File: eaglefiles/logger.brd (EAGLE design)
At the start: 41 x 20.2 mm, 15 parts, among them IC2 MAX641CSA

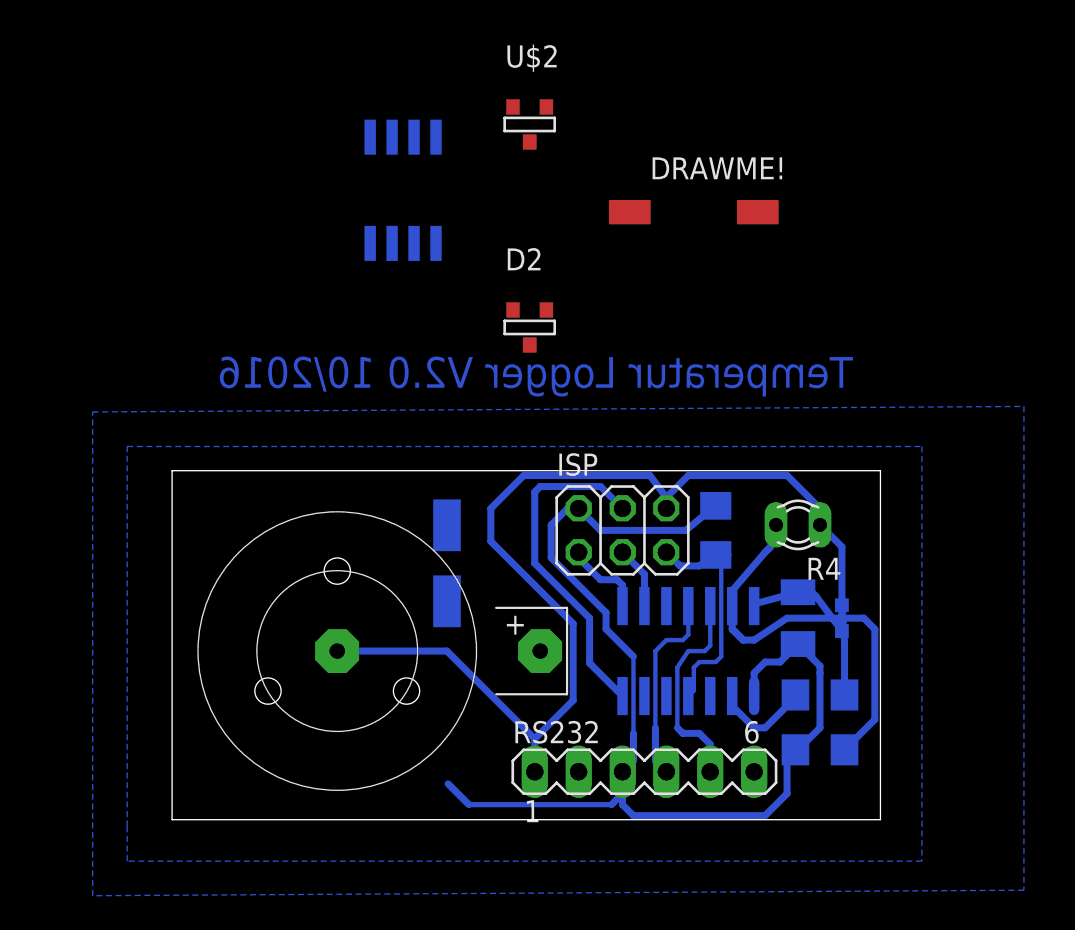
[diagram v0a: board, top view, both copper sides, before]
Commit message: UART-USB Adapter and TSIC-506 added
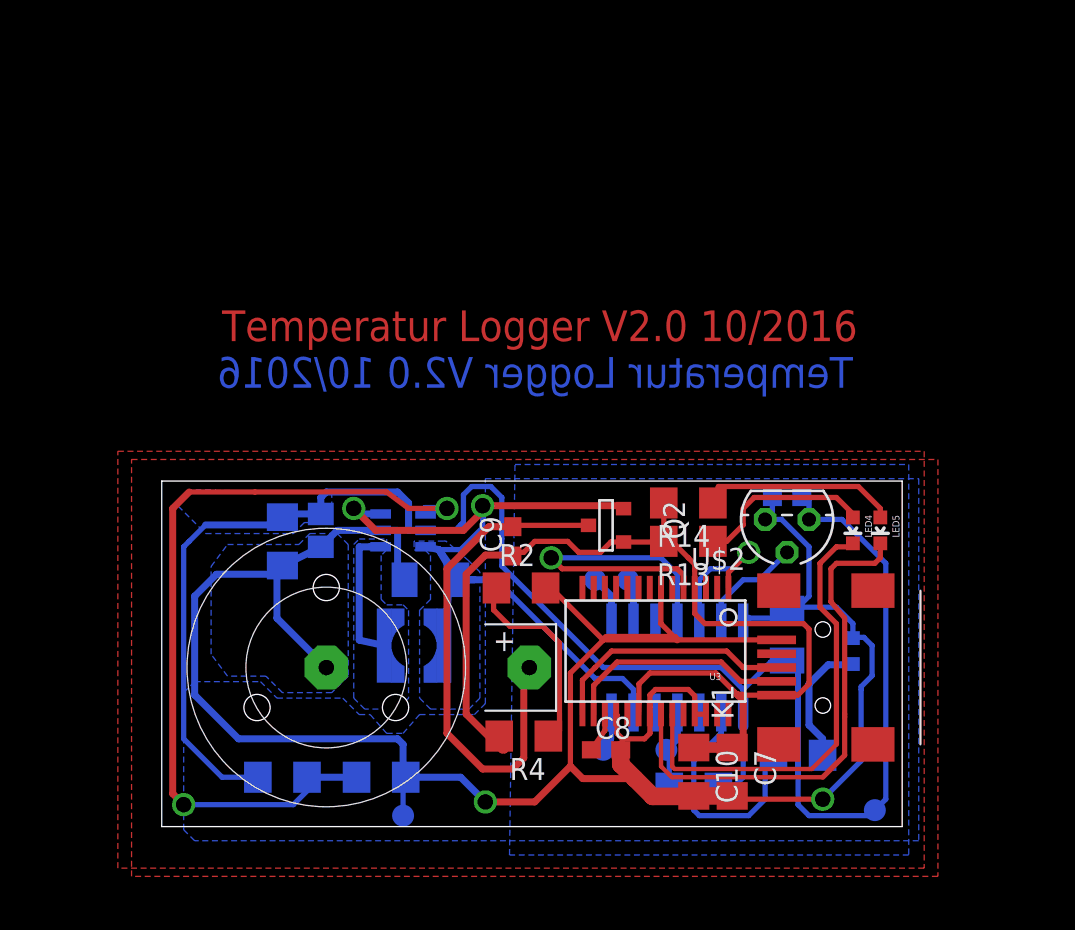
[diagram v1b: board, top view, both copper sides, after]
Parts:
- removed D2: BAV99, 0liver:SOT-23
- removed DRAWME!: 18uH, rcl:L8530M
- removed IC2: MAX641CSA, maxim:SO08
- removed ISP: (no value), pinhead:2X03
- removed RS232: (no value), con-lstb:MA06-1
- added C10: 10uF, rcl:C1206
- added C3: 4,7uF, rcl:C1206K
- added C4: 680nF, resistor:C0805
- added C5, C8, C9: 100nF, rcl:C0603
- added C7: 100nF, rcl:C1206
- added K1: 65100516121, Input-Output_Connectors_rev15d:65100516121
- added L1: 4,7uH, EagleLibrary_Wuerth_Elektronik_eiSos_rev16a:WE-TPC_3816
- added LED4: Red, SparkFun:LED-0603
- added LED5: Green, SparkFun:LED-0603
- added Q2: IRLML9301, 0liver:SOT-23
- added R13, R14: 1K, rcl:R1206
- added R5, R6: (no value), resistor:R1206
- added U$10, U$11, U$12, U$7, U$8, U$9: (no value), 0liver:PIN-1.27
- added U1: MCP1640, karlnet-parts:SOT23-6
- added U3: FT232RLSSOP, SparkFun:SSOP28DB
- C1: value 100uF -> 47uF; device rcl:153CLV-0505 -> resistor:C1206
- LED3: value (none) -> lc green; device led:SML0603 -> led:CHIPLED_0603
- R2: device rcl:R1206 -> eagle-ltspice:R1206
- R3: value 2k (calc!) -> 1,8k
- R4: value (none) -> 680; device ptc-ntc:P640 -> eagle-ltspice:R1206
- U$2: value IRLML6346 -> TSIC-506; device 0liver:SOT-23 -> 0liver:TO92
- moved U$2 27.3 mm to (36.2, 17.8), turned to 180 degrees
- moved R4 20.0 mm to (21.0, 5.24)
- moved R2 19.7 mm to (20.8, 13.8), flipped to the top
- moved R1 15.0 mm to (30.8, 2.22), turned to 180 degrees
- moved C1 9.61 mm to (6.99, 16.5), turned to 270 degrees
- moved R3 3.72 mm to (36.8, 4.13)
- moved LED3 2.01 mm to (40.0, 10.2), turned to 0 degrees
- moved IC1 1.14 mm to (29.8, 9.21)
- moved U$1 1.14 mm to (9.53, 9.21)
- moved C2 1.14 mm to (36.2, 11.1)
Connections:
- removed net D1: IC1.10, U$1.P$2
- removed net N$8: D2.3, DRAWME!.1, U$2.1
- new net 5V: R2.1, R4.1
- new net N$3: C8.1, U3.17
- new net N$4: LED4.A, R13.1
- new net N$6: C9.2, Q2.1, U$1.P$2
- new net RXLED: LED5.C, U3.22
- new net SW: L1.2, U1.1
- new net TXLED: LED4.C, U3.23
- new net USB_D+: K1.3, U3.15
- new net USB_D-: K1.2, U3.16
- new net VSUPPLY: C3.1, IC1.6, L1.1, Q2.2, U1.3, U1.6
- new net V_USB: C10.1, C7.1, C9.1, K1.1, Q2.3, R13.2, R14.2, R4.2, U3.20, U3.4
- net GND: now also C1.2, C10.2, C3.2, C4.2, C5.2, C7.2, C8.2, K1.5, R2.2, R6.1, U$10.P$1, U$2.3, U1.2, U3.18, U3.21, U3.25, U3.26, U3.7; no longer C1.-, IC2.1, IC2.3, IC2.7, ISP.6, R4.1, RS232.1, U$2.2
- net MISO: now also U$7.P$1; no longer ISP.1
- net MOSI: now also U$11.P$1; no longer ISP.4
- net N$1: now also U3.5; no longer RS232.4
- net N$2: now also U$2.2; no longer R2.1, R4.2
- net N$32: now also U3.1; no longer RS232.5
- net N$5: now also R5.1, R6.2, U1.4; no longer IC2.6, U$2.3
- net N$7: now also LED5.A, R14.1; no longer DRAWME!.2
- net RES: now also U$9.P$1; no longer ISP.5
- net SCK: now also U$8.P$1; no longer ISP.3
- net VCC: now also C1.1, C4.1, C5.1, R5.2, U$12.P$1, U$2.1, U1.5; no longer C1.+, D2.1, IC2.5, ISP.2, R2.2, RS232.3
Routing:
- net GND: track 69.0 -> 146.3 mm, vias 0 -> 2
- net V_USB: track 0.00 -> 61.1 mm
- net VSUPPLY: track 0.00 -> 48.8 mm, vias 0 -> 2
- net N$5: track 0.00 -> 48.1 mm, vias 0 -> 2
- net VCC: track 66.5 -> 114.0 mm
- net N$6: track 0.00 -> 30.1 mm
- net RXLED: track 0.00 -> 29.5 mm
- net TXLED: track 0.00 -> 26.4 mm
- net N$2: track 25.1 -> 6.20 mm
- net MOSI: track 19.7 -> 2.32 mm
- net USB_D+: track 0.00 -> 14.3 mm
- net USB_D-: track 0.00 -> 13.3 mm
- net 5V: track 0.00 -> 11.7 mm
- net N$7: track 0.00 -> 11.4 mm
- net N$4: track 0.00 -> 10.3 mm
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- added copper zone on layer 1, net FILL
- added copper zone on layer 1, net GND
- added copper zone on layer 16, net SW
- added copper zone on layer 16, net VCC
- added copper zone on layer 16, net VSUPPLY
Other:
- board size 41 x 20.2 mm -> 42.9 x 20 mm

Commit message: Added ctr for reset
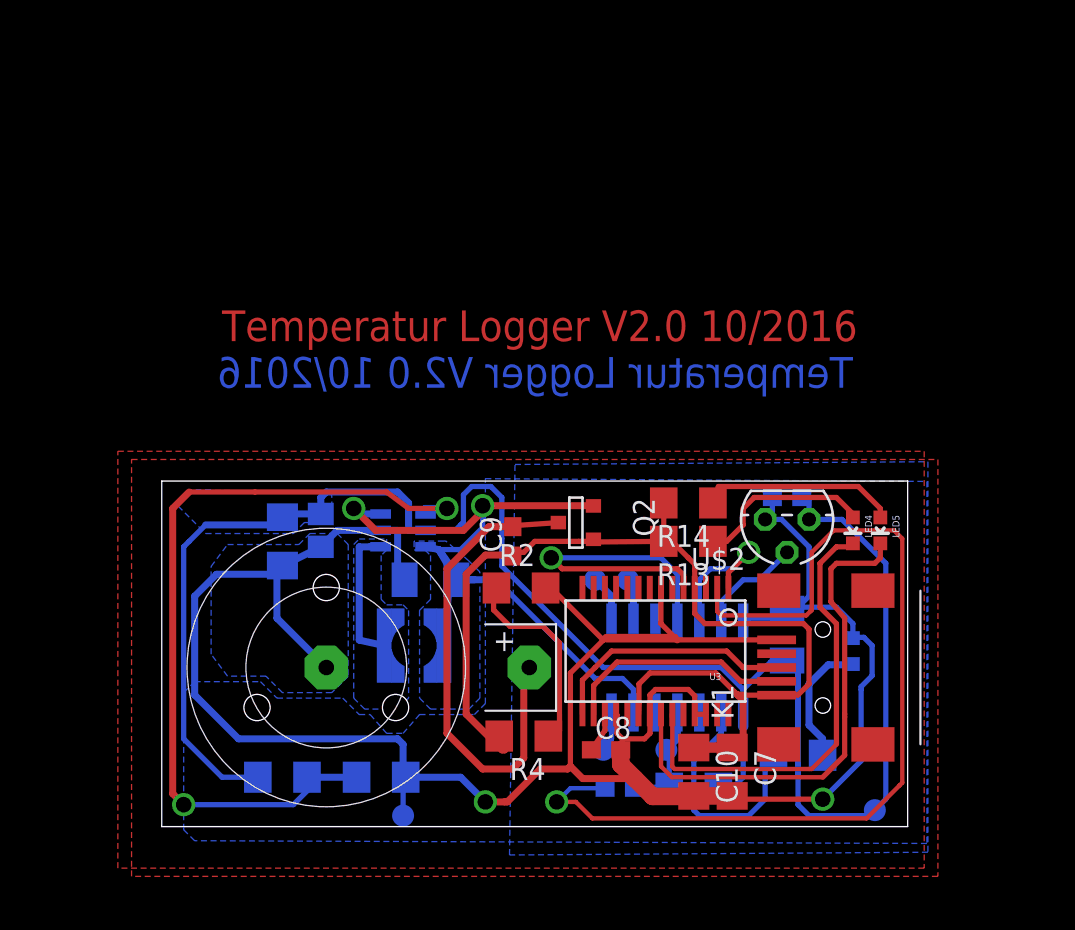
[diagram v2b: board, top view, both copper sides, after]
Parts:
- added C6: 100nF, rcl:C0603
- moved Q2 1.75 mm to (24.0, 17.6)
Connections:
- new net N$8: C6.2, U3.2
- net RES: now also C6.1
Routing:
- net N$8: track 0.00 -> 55.0 mm, vias 0 -> 1
- net RES: track 4.71 -> 6.73 mm
- net VSUPPLY: track 48.8 -> 47.0 mm
- net N$6: track 30.1 -> 28.4 mm
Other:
- board size 42.9 x 20 mm -> 43.2 x 20 mm
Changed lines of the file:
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@@
 <setting verticaltext="up"/>
 </settings>
-<grid distance="6.25" unitdist="mil" unit="mm" style="lines" multiple="1" display="no" altdistance="1.5625" altunitdist="mil" altunit="mil"/>
+<grid distance="6.25" unitdist="mil" unit="mil" style="lines" multiple="1" display="no" altdistance="1.5625" altunitdist="mil" altunit="mil"/>
 <layers>
 <layer number="1" name="Top" color="4" fill="1" visible="yes" active="yes"/>
@@
 <board>
 <plain>
-<wire x1="0" y1="0" x2="42.8575" y2="0" width="0" layer="20"/>
-<wire x1="42.8575" y1="0" x2="42.8575" y2="20" width="0" layer="20"/>
-<wire x1="42.8575" y1="20" x2="0" y2="20" width="0" layer="20"/>
+<wire x1="0" y1="0" x2="43.175" y2="0" width="0" layer="20"/>
+<wire x1="43.175" y1="0" x2="43.175" y2="20" width="0" layer="20"/>
+<wire x1="43.175" y1="20" x2="0" y2="20" width="0" layer="20"/>
 <text x="40.005" y="25.4" size="1.778" layer="16" rot="MR0">Temperatur Logger V2.0 10/2016</text>
 <wire x1="0" y1="0" x2="0" y2="20" width="0" layer="20"/>
@@
 <circle x="18.574" y="18.574" radius="0.35" width="0.3" layer="116"/>
 <text x="3.4925" y="28.09875" size="1.778" layer="1">Temperatur Logger V2.0 10/2016</text>
+<circle x="22.8605" y="1.429" radius="0.35" width="0.3" layer="116"/>
 </plain>
 <attributes>
@@
 <element name="C7" library="rcl" package="C1206" value="100nF" x="33.02" y="3.175" rot="R270"/>
 <element name="C8" library="rcl" package="C0603" value="100nF" x="25.7175" y="4.445"/>
-<element name="Q2" library="0liver" package="SOT-23" value="IRLML9301" x="25.7175" y="17.4625" rot="R270"/>
+<element name="Q2" library="0liver" package="SOT-23" value="IRLML9301" x="23.97125" y="17.62125" rot="R270"/>
 <element name="R2" library="eagle-ltspice" package="R1206" value="100k" x="20.79625" y="13.81125">
 <attribute name="SPICEPREFIX" value="R" x="20.79625" y="13.81125" size="1.778" layer="27" display="off"/>
@@
 </element>
 <element name="C10" library="rcl" package="C1206" value="10uF" x="30.7975" y="3.175" rot="R270"/>
+<element name="C6" library="rcl" package="C0603" value="100nF" x="26.51125" y="2.2225" rot="MR0"/>
 </elements>
 <signals>
@@
 <vertex x="18.7325" y="7.12"/>
 <vertex x="18.7325" y="20.1375"/>
-<vertex x="43.815" y="20.1375"/>
-<vertex x="43.815" y="-0.8175"/>
+<vertex x="44.29125" y="19.97875"/>
+<vertex x="44.29125" y="-0.97625"/>
 <vertex x="1.905" y="-0.8175"/>
 <vertex x="1.27" y="-0.1825"/>
@@
 <wire x1="27.384375" y1="2.778125" x2="26.5675" y2="3.595" width="1.016" layer="1"/>
 <wire x1="26.5675" y1="3.595" x2="26.5675" y2="4.445" width="1.016" layer="1"/>
-<wire x1="23.65375" y1="3.4925" x2="21.59" y2="1.42875" width="0.4064" layer="1"/>
-<wire x1="21.59" y1="1.42875" x2="18.7325" y2="1.42875" width="0.4064" layer="1"/>
+<wire x1="19.84375" y1="1.42875" x2="18.7325" y2="1.42875" width="0.4064" layer="1"/>
 <via x="18.7325" y="1.42875" extent="1-16" drill="0.9" shape="octagon"/>
 <wire x1="18.7325" y1="1.42875" x2="17.30375" y2="2.8575" width="0.4064" layer="16"/>
@@
 <wire x1="22.21825" y1="13.81125" x2="22.5425" y2="13.81125" width="0.3048" layer="1"/>
 <wire x1="22.5425" y1="13.81125" x2="25.55875" y2="10.795" width="0.3048" layer="1"/>
+<wire x1="19.84375" y1="1.42875" x2="20.0025" y2="1.42875" width="0.4064" layer="1"/>
+<wire x1="20.0025" y1="1.42875" x2="21.9075" y2="3.33375" width="0.4064" layer="1"/>
+<wire x1="21.9075" y1="3.33375" x2="23.495" y2="3.33375" width="0.4064" layer="1"/>
+<wire x1="23.495" y1="3.33375" x2="23.65375" y2="3.4925" width="0.4064" layer="1"/>
 </signal>
 <signal name="VSUPPLY">
@@
 <wire x1="16.8275" y1="14.9225" x2="16.03375" y2="16.03375" width="0.4064" layer="16"/>
 <via x="18.57375" y="18.57375" extent="1-16" drill="0.9" shape="octagon"/>
-<wire x1="18.57375" y1="18.57375" x2="26.56205" y2="18.57375" width="0.4064" layer="1"/>
-<wire x1="26.56205" y1="18.57375" x2="26.7335" y2="18.4023" width="0.4064" layer="1" curve="-90"/>
+<wire x1="18.57375" y1="18.57375" x2="24.97455" y2="18.57375" width="0.4064" layer="1"/>
+<wire x1="24.97455" y1="18.57375" x2="24.98725" y2="18.56105" width="0.4064" layer="1" curve="-90"/>
 <wire x1="11.1125" y1="18.415" x2="12.3825" y2="17.145" width="0.4064" layer="1"/>
 <wire x1="12.3825" y1="17.145" x2="17.4625" y2="17.145" width="0.4064" layer="1"/>
@@
 <wire x1="29.21" y1="4.445" x2="29.3755" y2="4.2795" width="0.3048" layer="16"/>
 <wire x1="29.3755" y1="4.2795" x2="29.3755" y2="2.2225" width="0.3048" layer="16"/>
+<contactref element="C6" pad="1"/>
+<wire x1="27.36125" y1="2.2225" x2="29.3755" y2="2.2225" width="0.4064" layer="16"/>
 </signal>
 <signal name="VCC">
@@
 <polygon width="0.4064" layer="16">
 <vertex x="20.4475" y="20.96"/>
-<vertex x="43.2375" y="20.96"/>
-<vertex x="43.2375" y="-1.6425"/>
+<vertex x="44.34875" y="21.11875"/>
+<vertex x="44.34875" y="-1.48375"/>
 <vertex x="20.13" y="-1.6425"/>
 </polygon>
@@
 <wire x1="36.83" y1="7.62" x2="37.465" y2="8.255" width="0.3048" layer="1"/>
 <wire x1="37.465" y1="8.255" x2="37.465" y2="11.43" width="0.3048" layer="1"/>
-<wire x1="26.7335" y1="16.4719" x2="29.0199" y2="16.4719" width="0.3048" layer="1"/>
-<wire x1="29.0199" y1="16.4719" x2="29.058" y2="16.51" width="0.3048" layer="1"/>
+<wire x1="24.98725" y1="16.63065" x2="24.8924" y2="16.4719" width="0.3048" layer="1"/>
+<wire x1="24.8924" y1="16.4719" x2="29.058" y2="16.51" width="0.3048" layer="1"/>
 <wire x1="29.058" y1="16.51" x2="29.5275" y2="16.51" width="0.3048" layer="1"/>
 <wire x1="29.5275" y1="16.51" x2="30.48" y2="15.5575" width="0.3048" layer="1"/>
 <wire x1="30.85" y1="13.816" x2="30.85" y2="14.87" width="0.3048" layer="1"/>
 <wire x1="29.058" y1="18.7325" x2="29.058" y2="16.51" width="0.3048" layer="1"/>
-<wire x1="26.7335" y1="16.4719" x2="25.9969" y2="16.4719" width="0.3048" layer="1"/>
-<wire x1="25.9969" y1="16.4719" x2="25.4" y2="15.875" width="0.3048" layer="1"/>
-<wire x1="25.4" y1="15.875" x2="24.13" y2="15.875" width="0.3048" layer="1"/>
-<wire x1="24.13" y1="15.875" x2="23.495" y2="16.51" width="0.3048" layer="1"/>
+<wire x1="24.98725" y1="16.63065" x2="24.88565" y2="16.63065" width="0.3048" layer="1"/>
+<wire x1="24.88565" y1="16.63065" x2="24.92375" y2="16.51" width="0.3048" layer="1"/>
+<wire x1="24.92375" y1="16.51" x2="24.13" y2="16.51" width="0.3048" layer="1"/>
+<wire x1="24.13" y1="16.51" x2="23.495" y2="16.51" width="0.3048" layer="1"/>
 <wire x1="23.495" y1="16.51" x2="21.59" y2="16.51" width="0.3048" layer="1"/>
 <wire x1="21.59" y1="16.51" x2="20.955" y2="15.875" width="0.3048" layer="1"/>
@@
 <contactref element="Q2" pad="1"/>
 <contactref element="C9" pad="2"/>
-<wire x1="24.7015" y1="17.4371" x2="20.6121" y2="17.4371" width="0.3048" layer="1"/>
+<wire x1="22.95525" y1="17.59585" x2="20.6121" y2="17.4371" width="0.3048" layer="1"/>
 <wire x1="20.6121" y1="17.4371" x2="20.6375" y2="17.4625" width="0.3048" layer="1"/>
 <wire x1="20.6375" y1="17.4625" x2="20.4225" y2="17.4625" width="0.3048" layer="1"/>
@@
 <wire x1="19.20875" y1="13.64575" x2="19.37425" y2="13.81125" width="0.3048" layer="1"/>
 </signal>
+<signal name="N$8">
+<contactref element="U3" pad="2"/>
+<contactref element="C6" pad="2"/>
+<wire x1="32.15" y1="13.816" x2="32.15" y2="12.45875" width="0.254" layer="1"/>
+<wire x1="32.15" y1="12.45875" x2="32.385" y2="12.22375" width="0.254" layer="1"/>
+<wire x1="32.385" y1="12.22375" x2="37.30625" y2="12.22375" width="0.254" layer="1"/>
+<wire x1="37.30625" y1="12.22375" x2="37.544375" y2="12.461875" width="0.254" layer="1"/>
+<wire x1="37.544375" y1="12.461875" x2="37.62375" y2="12.54125" width="0.254" layer="1"/>
+<wire x1="25.66125" y1="2.2225" x2="23.65375" y2="2.2225" width="0.254" layer="16"/>
+<wire x1="23.65375" y1="2.2225" x2="22.86" y2="1.42875" width="0.254" layer="16"/>
+<via x="22.86" y="1.42875" extent="1-16" drill="0.9" diameter="1.016" shape="octagon"/>
+<wire x1="22.86" y1="1.42875" x2="23.97125" y2="1.42875" width="0.254" layer="1"/>
+<wire x1="23.97125" y1="1.42875" x2="24.92375" y2="0.47625" width="0.254" layer="1"/>
+<wire x1="24.92375" y1="0.47625" x2="40.79875" y2="0.47625" width="0.254" layer="1"/>
+<wire x1="40.79875" y1="0.47625" x2="42.70375" y2="2.38125" width="0.254" layer="1"/>
+<wire x1="42.70375" y1="2.38125" x2="42.8625" y2="2.54" width="0.254" layer="1"/>
+<wire x1="42.8625" y1="2.54" x2="42.8625" y2="16.66875" width="0.254" layer="1"/>
+<wire x1="42.8625" y1="16.66875" x2="42.38625" y2="17.145" width="0.254" layer="1"/>
+<wire x1="42.38625" y1="17.145" x2="38.89375" y2="17.145" width="0.254" layer="1"/>
+<wire x1="38.89375" y1="17.145" x2="37.62375" y2="15.875" width="0.254" layer="1"/>
+<wire x1="37.62375" y1="15.875" x2="37.62375" y2="12.54125" width="0.254" layer="1"/>
+<wire x1="37.62375" y1="12.54125" x2="37.544375" y2="12.461875" width="0.254" layer="1"/>
+</signal>
 </signals>
